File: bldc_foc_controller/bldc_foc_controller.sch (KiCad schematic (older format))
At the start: 197 parts, among them J1 Conn_01x05, J2 Conn_02x19_Odd_Even, J3 Conn_02x19_Odd_Even, J4 Conn_01x10, J5 CONN_01x02, J6 CONN_01X03, J7 CONN_01x02, J8 CONN_01x02, Q1 HYG025N06LS1C2, Q10 PSMN2R2-40YSD, Q11 DNP, Q12 DNP, Q13 PSMN2R2-40YSD, Q14 PSMN2R2-40YSD, Q15 DNP, Q16 DNP, Q2 HYG025N06LS1C2, Q3 HYG025N06LS1C2, Q4 HYG025N06LS1C2, Q5 PSMN2R2-40YSD, Q6 PSMN2R2-40YSD, Q7 DNP, Q8 DNP, Q9 PSMN2R2-40YSD, U1 redcube-7461057, U10 INA240A1D, U11 INA240A1D, U12 DRV8320S, U13 INA240A1D, U2 redcube-7461057, U3 redcube-7461057, U4 TLS4120D0EPVXUMA1, U6 redcube-7461057, U7 LTC4368CMS-1-PBF, U8 LMP8481ASQDGKRQ1, U9 LMP8481ASQDGKRQ1

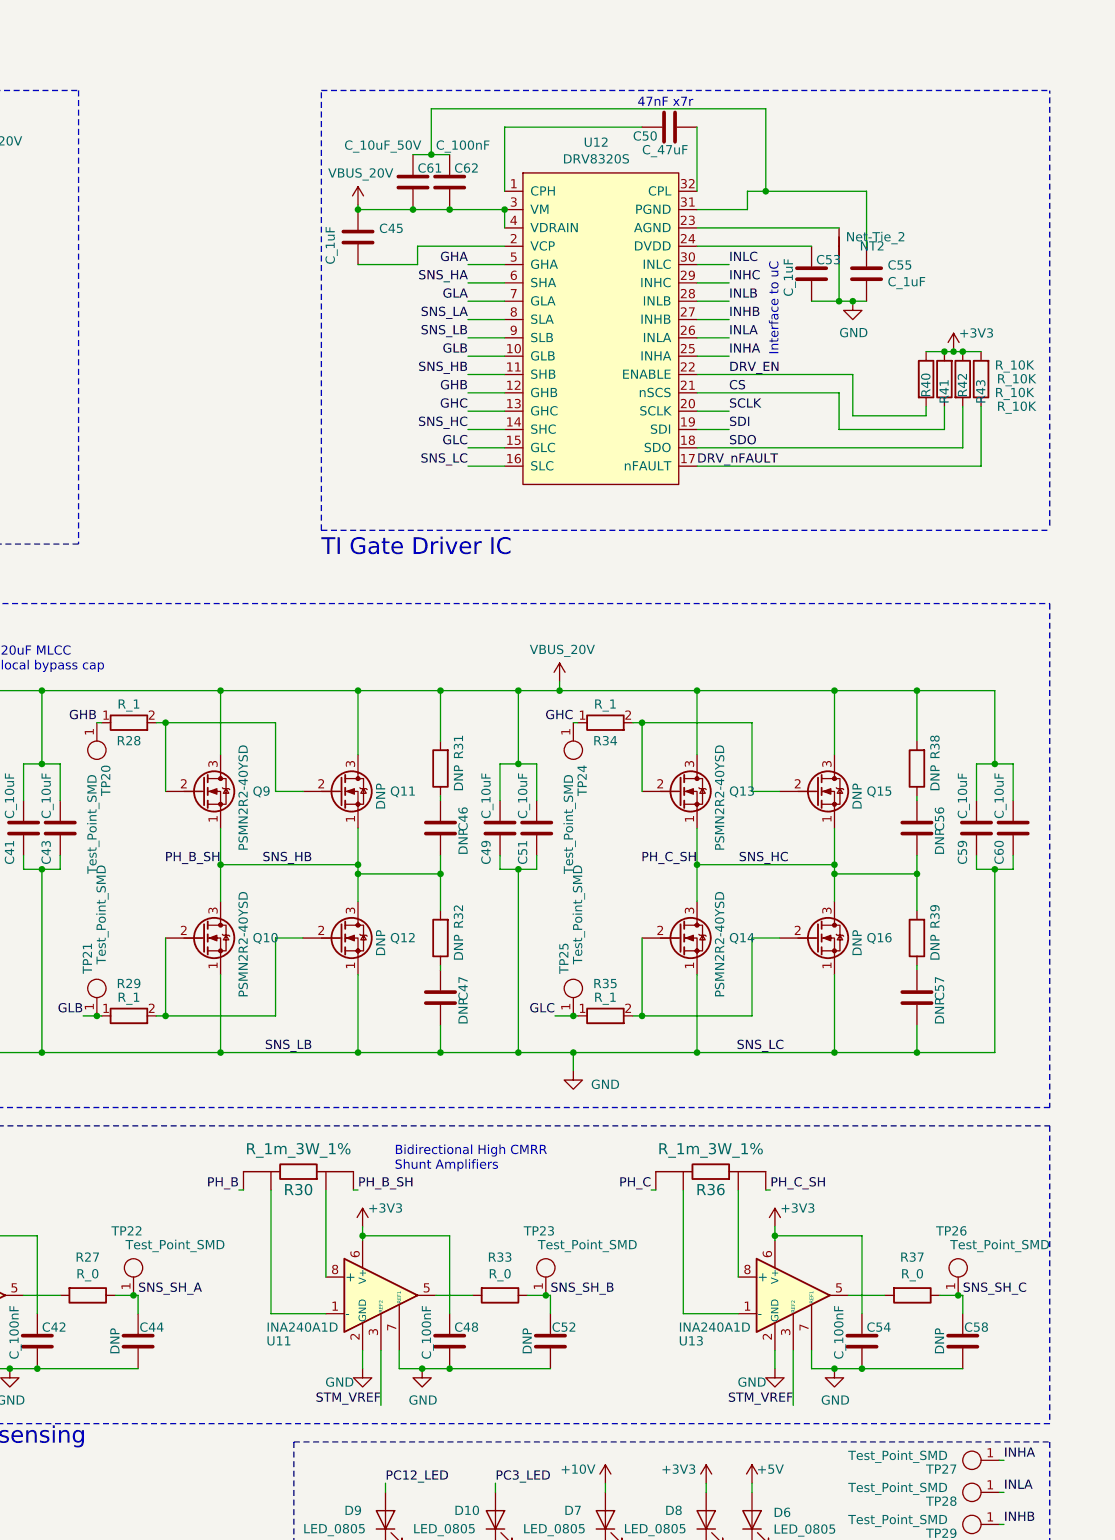
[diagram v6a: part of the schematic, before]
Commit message: moving comps to the board
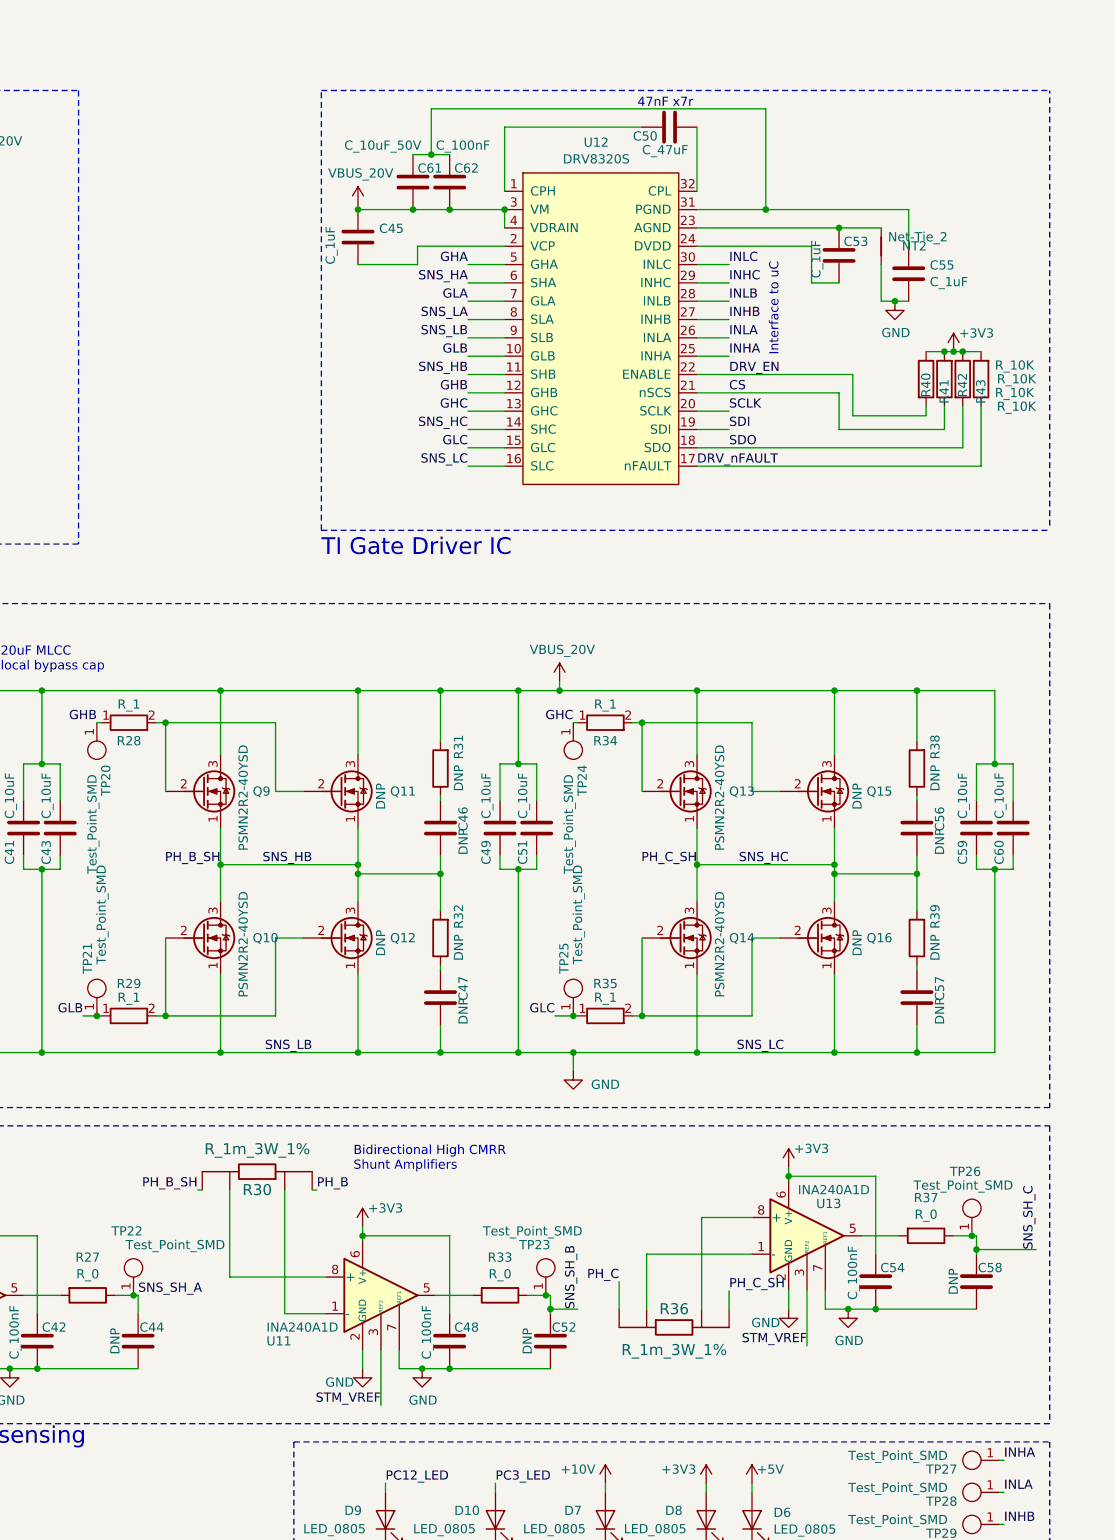
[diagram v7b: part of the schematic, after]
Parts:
- NT2: footprint (none) -> NetTie:NetTie-2_SMD_Pad0.5mm
- R36: footprint formula:WSL27261L000FEB -> footprints:WSL27261L000FEB
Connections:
- net GND: no longer C53.2
- net PH_B: now also R30.4; no longer R30.1
- net PH_B_SH: now also R30.1; no longer R30.4
- net PH_C: now also R36.4; no longer R36.1
- net PH_C_SH: now also R36.1; no longer R36.4
- net at U11.1 (-): now also R30.3; no longer R30.2
- net at U11.8 (+): now also R30.2; no longer R30.3
- net at R36.2: now also U13.8 (+); no longer U13.1 (-)
- net at R36.3: now also U13.1 (-); no longer U13.8 (+)
- net at NT2.1, U12.23 (AGND): now also C53.1
- net at U12.24 (DVDD): now also C53.2; no longer C53.1
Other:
- moved on the sheet: C53, C54, C55, C58, NT2, R30, R37, TP26, U13

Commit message: housekeeping
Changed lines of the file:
@@
 Wire Wire Line
 	14575 7475 14800 7475
+Entry Wire Line
+	20000 8050 20100 8150
 $EndSCHEMATC
